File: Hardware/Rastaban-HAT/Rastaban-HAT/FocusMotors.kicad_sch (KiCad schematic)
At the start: 10 parts, among them U6 TMC2208_Carrier, U7 DRV8838 POLOLU, U8 TLV1117-33

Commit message: enh pcb component layout
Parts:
- C14, C15, C18, C19, C24: Purpose (none) -> decoupling
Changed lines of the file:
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@@
+      (effects (font (size 1.27 1.27)) hide)
+    )
+    (property "Purpose" "decoupling" (id 4) (at 193.04 111.125 0)
       (effects (font (size 1.27 1.27)) hide)
     )
@@
       (effects (font (size 1.27 1.27)) hide)
     )
+    (property "Purpose" "decoupling" (id 4) (at 201.295 109.855 0)
+      (effects (font (size 1.27 1.27)) hide)
+    )
     (pin "1")
     (pin "2")
@@
     )
     (property "Manufacturer_Part_Number" "C525005" (id 5) (at 134.62 106.68 0)
+      (effects (font (size 1.27 1.27)) hide)
+    )
+    (property "Purpose" "decoupling" (id 6) (at 134.62 106.68 0)
       (effects (font (size 1.27 1.27)) hide)
     )
@@
       (effects (font (size 1.27 1.27)) hide)
     )
+    (property "Purpose" "decoupling" (id 4) (at 126.365 99.06 0)
+      (effects (font (size 1.27 1.27)) hide)
+    )
     (pin "1")
     (pin "2")
@@
       (effects (font (size 1.27 1.27)) hide)
     )
+    (property "Purpose" "decoupling" (id 6) (at 170.18 111.125 0)
+      (effects (font (size 1.27 1.27)) hide)
+    )

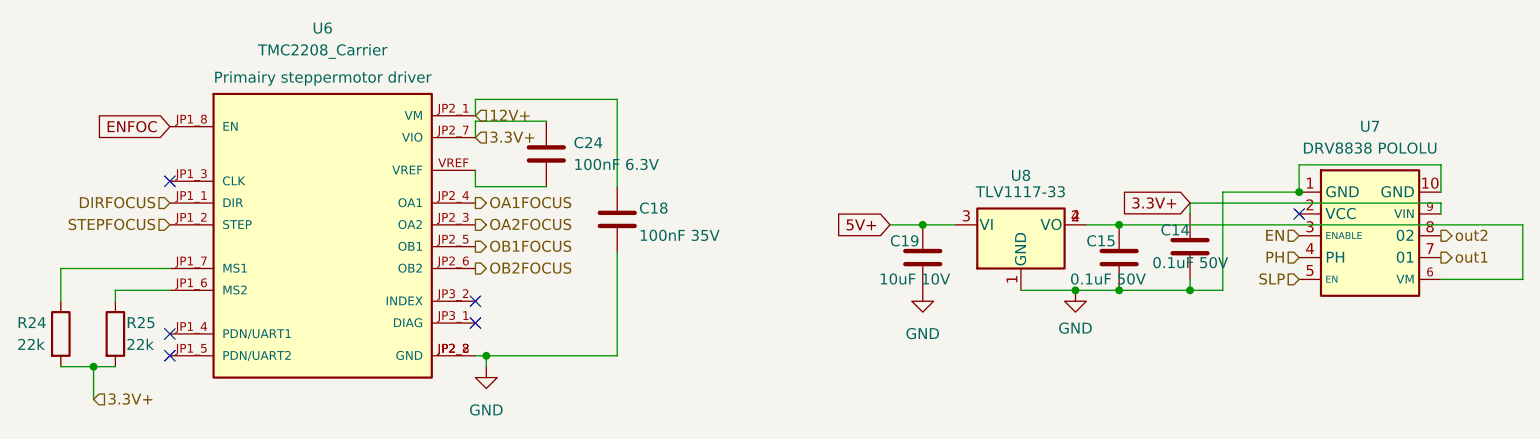
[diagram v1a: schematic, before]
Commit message: changed capacitor footprints
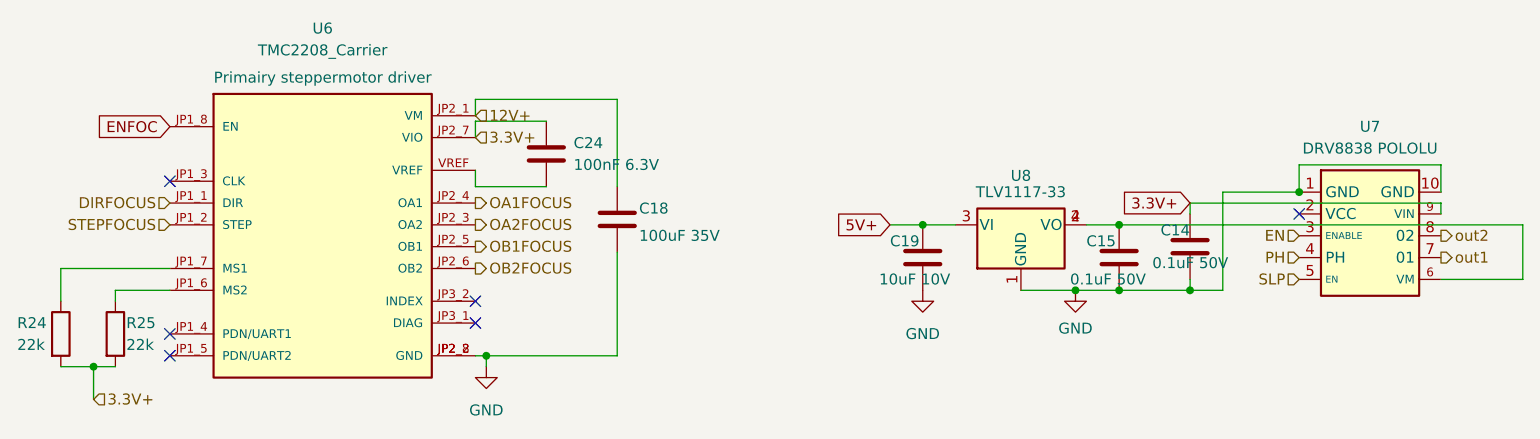
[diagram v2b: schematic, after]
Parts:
- C14, C15: footprint Capacitor_SMD:C_0805_2012Metric_Pad1.18x1.45mm_HandSolder -> Capacitor_SMD:CP_Elec_6.3x7.7
- C18: value 100nF 35V -> 100uF 35V; footprint Capacitor_THT:C_Radial_D6.3mm_H11.0mm_P2.50mm -> Capacitor_SMD:CP_Elec_8x10
- C19: footprint Capacitor_THT:C_Radial_D6.3mm_H11.0mm_P2.50mm -> Capacitor_SMD:CP_Elec_3x5.4
- C24: footprint Capacitor_SMD:C_0805_2012Metric_Pad1.18x1.45mm_HandSolder -> Capacitor_SMD:CP_Elec_4x5.4
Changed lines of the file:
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@@
       (effects (font (size 1.27 1.27)) (justify right))
     )
-    (property "Footprint" "Capacitor_SMD:C_0805_2012Metric_Pad1.18x1.45mm_HandSolder" (id 2) (at 192.0748 107.315 0)
+    (property "Footprint" "Capacitor_SMD:CP_Elec_6.3x7.7" (id 2) (at 192.0748 107.315 0)
       (effects (font (size 1.27 1.27)) hide)
     )
@@
       (effects (font (size 1.27 1.27)) (justify right))
     )
-    (property "Footprint" "Capacitor_SMD:C_0805_2012Metric_Pad1.18x1.45mm_HandSolder" (id 2) (at 202.2602 113.665 0)
+    (property "Footprint" "Capacitor_SMD:CP_Elec_6.3x7.7" (id 2) (at 202.2602 113.665 0)
       (effects (font (size 1.27 1.27)) hide)
     )
@@
       (effects (font (size 1.27 1.27)) (justify left))
     )
-    (property "Value" "100nF 35V" (id 1) (at 137.16 108.585 0)
-      (effects (font (size 1.27 1.27)) (justify left))
-    )
-    (property "Footprint" "Capacitor_THT:C_Radial_D6.3mm_H11.0mm_P2.50mm" (id 2) (at 135.5852 110.49 0)
+    (property "Value" "100uF 35V" (id 1) (at 137.16 108.585 0)
+      (effects (font (size 1.27 1.27)) (justify left))
+    )
+    (property "Footprint" "Capacitor_SMD:CP_Elec_8x10" (id 2) (at 135.5852 110.49 0)
       (effects (font (size 1.27 1.27)) hide)
     )
@@
       (effects (font (size 1.27 1.27)) (justify left))
     )
-    (property "Footprint" "Capacitor_SMD:C_0805_2012Metric_Pad1.18x1.45mm_HandSolder" (id 2) (at 127.3302 102.87 0)
+    (property "Footprint" "Capacitor_SMD:CP_Elec_4x5.4" (id 2) (at 127.3302 102.87 0)
       (effects (font (size 1.27 1.27)) hide)
     )
@@
       (effects (font (size 1.27 1.27)) (justify left))
     )
-    (property "Footprint" "Capacitor_THT:C_Radial_D6.3mm_H11.0mm_P2.50mm" (id 2) (at 171.1452 114.935 0)
-      (effects (font (size 1.27 1.27)) hide)
-    )
+    (property "Footprint" "Capacitor_SMD:CP_Elec_3x5.4" (id 2) (at 171.1452 114.935 0)
+      (effects (font (size 1.27 1.27)) hide)
+    )

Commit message: added testpoints
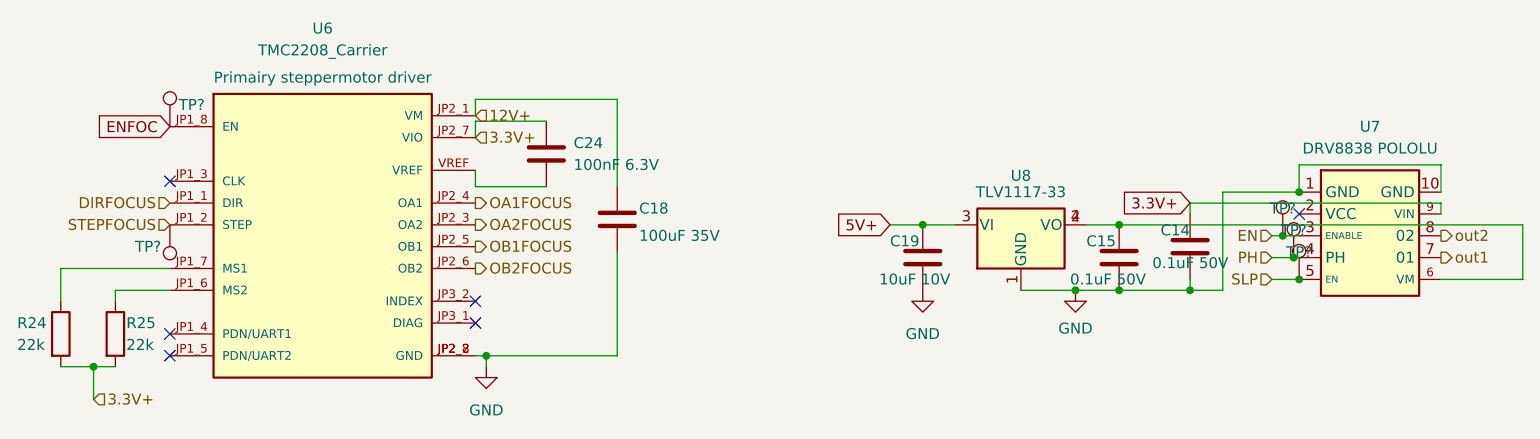
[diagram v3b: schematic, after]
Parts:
- added TP? (x5): TestPoint, TestPoint:TestPoint_THTPad_2.0x2.0mm_Drill1.0mm, symbol Connector:TestPoint
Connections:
- net EN: now also TP?.1
- net ENFOC: now also TP?.1
- net PH: now also TP?.1
- net SLP: now also TP?.1
- net STEPFOCUS: now also TP?.1
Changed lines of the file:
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@@
     (comment 1 "Casper R. Tak")
   )
+  (junction (at 213.995 113.665) (diameter 0) (color 0 0 0 0)
+  )
   (junction (at 119.38 122.555) (diameter 0) (color 0 0 0 0)
   )
@@
   (junction (at 213.995 103.505) (diameter 0) (color 0 0 0 0)
   )
+  (junction (at 212.09 108.585) (diameter 0) (color 0 0 0 0)
+  )
   (junction (at 170.18 107.315) (diameter 0) (color 0 0 0 0)
   )
   (junction (at 187.96 114.935) (diameter 0) (color 0 0 0 0)
+  )
+  (junction (at 213.36 111.125) (diameter 0) (color 0 0 0 0)
   )
   (junction (at 201.295 114.935) (diameter 0) (color 0 0 0 0)
@@
     (stroke (width 0) (type default) (color 0 0 0 0))
   )
+  (wire (pts (xy 213.36 111.125) (xy 213.995 111.125))
+    (stroke (width 0) (type default) (color 0 0 0 0))
+  )
   (wire (pts (xy 230.505 104.775) (xy 230.505 106.045))
     (stroke (width 0) (type default) (color 0 0 0 0))
@@
     (stroke (width 0) (type default) (color 0 0 0 0))
   )
+  (wire (pts (xy 212.09 108.585) (xy 213.995 108.585))
+    (stroke (width 0) (type default) (color 0 0 0 0))
+  )
   (wire (pts (xy 118.11 100.965) (xy 118.11 102.87))
     (stroke (width 0) (type default) (color 0 0 0 0))
@@
     (stroke (width 0) (type default) (color 0 0 0 0))
   )
+  (wire (pts (xy 210.82 113.665) (xy 213.995 113.665))
+    (stroke (width 0) (type default) (color 0 0 0 0))
+  )
   (wire (pts (xy 118.11 95.25) (xy 118.11 97.155))
     (stroke (width 0) (type default) (color 0 0 0 0))
@@
     (stroke (width 0) (type default) (color 0 0 0 0))
   )
+  (wire (pts (xy 210.82 111.125) (xy 213.36 111.125))
+    (stroke (width 0) (type default) (color 0 0 0 0))
+  )
   (wire (pts (xy 118.11 95.25) (xy 126.365 95.25))
     (stroke (width 0) (type default) (color 0 0 0 0))
@@
   )
   (wire (pts (xy 201.295 114.935) (xy 205.105 114.935))
+    (stroke (width 0) (type default) (color 0 0 0 0))
+  )
+  (wire (pts (xy 210.82 108.585) (xy 212.09 108.585))
     (stroke (width 0) (type default) (color 0 0 0 0))
   )
@@
     (effects (font (size 1.27 1.27)) (justify right))
   )
-  (hierarchical_label "SLP" (shape input) (at 213.995 113.665 180)
+  (hierarchical_label "SLP" (shape input) (at 210.82 113.665 180)
     (effects (font (size 1.27 1.27)) (justify right))
   )
@@
     (effects (font (size 1.27 1.27)) (justify left))
   )
-  (hierarchical_label "EN" (shape input) (at 213.995 108.585 180)
-    (effects (font (size 1.27 1.27)) (justify right))
-  )
-  (hierarchical_label "PH" (shape input) (at 213.995 111.125 180)
+  (hierarchical_label "EN" (shape input) (at 210.82 108.585 180)
+    (effects (font (size 1.27 1.27)) (justify right))
+  )
+  (hierarchical_label "PH" (shape input) (at 210.82 111.125 180)
     (effects (font (size 1.27 1.27)) (justify right))
   )
@@
     (pin "1")
     (pin "2")
+  )
+  (symbol (lib_id "Connector:TestPoint") (at 213.36 111.125 0) (unit 1)
+    (in_bom yes) (on_board yes)
+    (property "Reference" "TP?" (id 0) (at 213.36 107.95 0))
+    (property "Value" "TestPoint" (id 1) (at 213.36 106.045 0)
+      (effects (font (size 1.27 1.27)) hide)
+    )
+    (property "Footprint" "TestPoint:TestPoint_THTPad_2.0x2.0mm_Drill1.0mm" (id 2) (at 218.44 111.125 0)
+      (effects (font (size 1.27 1.27)) hide)
+    )
+    (property "Datasheet" "~" (id 3) (at 218.44 111.125 0)
+      (effects (font (size 1.27 1.27)) hide)
+    )
+    (pin "1")
   )
   (symbol (lib_id "power:GND") (at 170.18 114.935 0) (unit 1)
@@
     (pin "2")
   )
+  (symbol (lib_id "Connector:TestPoint") (at 212.09 108.585 0) (unit 1)
+    (in_bom yes) (on_board yes)
+    (property "Reference" "TP?" (id 0) (at 212.09 105.41 0))
+    (property "Value" "TestPoint" (id 1) (at 212.09 103.505 0)
+      (effects (font (size 1.27 1.27)) hide)
+    )
+    (property "Footprint" "TestPoint:TestPoint_THTPad_2.0x2.0mm_Drill1.0mm" (id 2) (at 217.17 108.585 0)
+      (effects (font (size 1.27 1.27)) hide)
+    )
+    (property "Datasheet" "~" (id 3) (at 217.17 108.585 0)
+      (effects (font (size 1.27 1.27)) hide)
+    )
+    (pin "1")
+  )
+  (symbol (lib_id "Connector:TestPoint") (at 82.55 107.315 180) (unit 1)
+    (in_bom yes) (on_board yes)
+    (property "Reference" "TP?" (id 0) (at 80.01 109.855 0))
+    (property "Value" "TestPoint" (id 1) (at 82.55 112.395 0)
+      (effects (font (size 1.27 1.27)) hide)
+    )
+    (property "Footprint" "TestPoint:TestPoint_THTPad_2.0x2.0mm_Drill1.0mm" (id 2) (at 77.47 107.315 0)
+      (effects (font (size 1.27 1.27)) hide)
+    )
+    (property "Datasheet" "~" (id 3) (at 77.47 107.315 0)
+      (effects (font (size 1.27 1.27)) hide)
+    )
+    (pin "1")
+  )
+  (symbol (lib_id "Connector:TestPoint") (at 82.55 95.885 0) (unit 1)
+    (in_bom yes) (on_board yes)
+    (property "Reference" "TP?" (id 0) (at 85.09 93.345 0))
+    (property "Value" "TestPoint" (id 1) (at 82.55 90.805 0)
+      (effects (font (size 1.27 1.27)) hide)
+    )
+    (property "Footprint" "TestPoint:TestPoint_THTPad_2.0x2.0mm_Drill1.0mm" (id 2) (at 87.63 95.885 0)
+      (effects (font (size 1.27 1.27)) hide)
+    )
+    (property "Datasheet" "~" (id 3) (at 87.63 95.885 0)
+      (effects (font (size 1.27 1.27)) hide)
+    )
+    (pin "1")
+  )
   (symbol (lib_id "Device:C") (at 126.365 99.06 0) (unit 1)
     (in_bom yes) (on_board yes) (fields_autoplaced)
@@
     (pin "2")
   )
+  (symbol (lib_id "Connector:TestPoint") (at 213.995 113.665 0) (unit 1)
+    (in_bom yes) (on_board yes)
+    (property "Reference" "TP?" (id 0) (at 213.995 110.49 0))
+    (property "Value" "TestPoint" (id 1) (at 213.995 108.585 0)
+      (effects (font (size 1.27 1.27)) hide)
+    )
+    (property "Footprint" "TestPoint:TestPoint_THTPad_2.0x2.0mm_Drill1.0mm" (id 2) (at 219.075 113.665 0)
+      (effects (font (size 1.27 1.27)) hide)
+    )
+    (property "Datasheet" "~" (id 3) (at 219.075 113.665 0)
+      (effects (font (size 1.27 1.27)) hide)
+    )
+    (pin "1")
+  )
   (symbol (lib_id "Device:R") (at 76.2 120.015 0) (unit 1)

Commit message: Removed LEDS
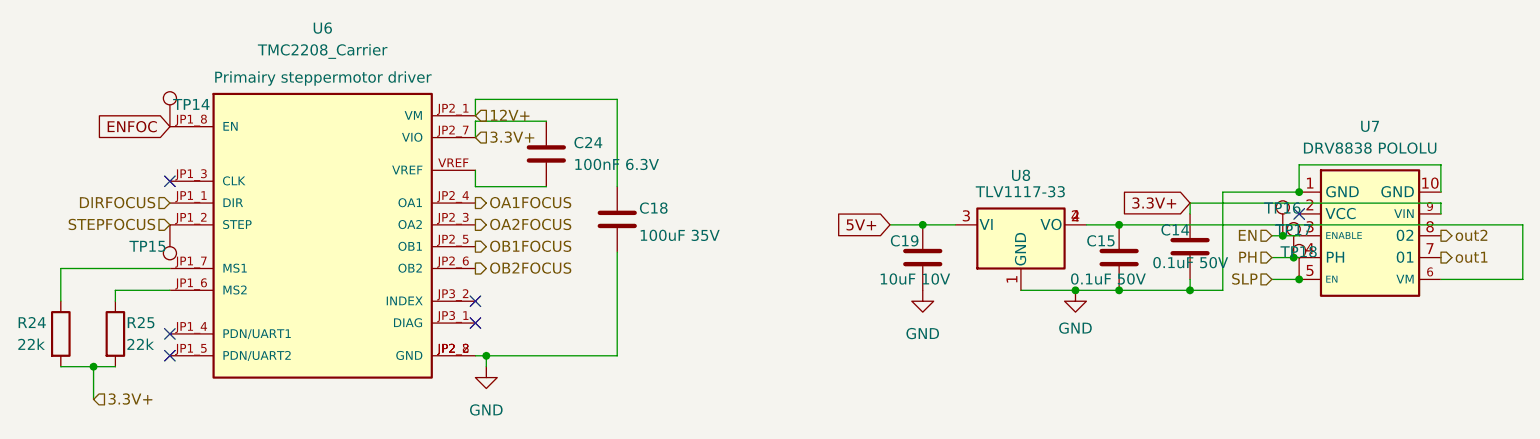
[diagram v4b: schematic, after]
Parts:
- gave numbers to parts that had none: 5
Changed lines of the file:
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@@
   (symbol (lib_id "Connector:TestPoint") (at 213.36 111.125 0) (unit 1)
     (in_bom yes) (on_board yes)
-    (property "Reference" "TP?" (id 0) (at 213.36 107.95 0))
+    (property "Reference" "TP17" (id 0) (at 213.36 107.95 0))
     (property "Value" "TestPoint" (id 1) (at 213.36 106.045 0)
       (effects (font (size 1.27 1.27)) hide)
@@
   (symbol (lib_id "Connector:TestPoint") (at 212.09 108.585 0) (unit 1)
     (in_bom yes) (on_board yes)
-    (property "Reference" "TP?" (id 0) (at 212.09 105.41 0))
+    (property "Reference" "TP16" (id 0) (at 212.09 105.41 0))
     (property "Value" "TestPoint" (id 1) (at 212.09 103.505 0)
       (effects (font (size 1.27 1.27)) hide)
@@
   (symbol (lib_id "Connector:TestPoint") (at 82.55 107.315 180) (unit 1)
     (in_bom yes) (on_board yes)
-    (property "Reference" "TP?" (id 0) (at 80.01 109.855 0))
+    (property "Reference" "TP15" (id 0) (at 80.01 109.855 0))
     (property "Value" "TestPoint" (id 1) (at 82.55 112.395 0)
       (effects (font (size 1.27 1.27)) hide)
@@
   (symbol (lib_id "Connector:TestPoint") (at 82.55 95.885 0) (unit 1)
     (in_bom yes) (on_board yes)
-    (property "Reference" "TP?" (id 0) (at 85.09 93.345 0))
+    (property "Reference" "TP14" (id 0) (at 85.09 93.345 0))
     (property "Value" "TestPoint" (id 1) (at 82.55 90.805 0)
       (effects (font (size 1.27 1.27)) hide)
@@
   (symbol (lib_id "Connector:TestPoint") (at 213.995 113.665 0) (unit 1)
     (in_bom yes) (on_board yes)
-    (property "Reference" "TP?" (id 0) (at 213.995 110.49 0))
+    (property "Reference" "TP18" (id 0) (at 213.995 110.49 0))
     (property "Value" "TestPoint" (id 1) (at 213.995 108.585 0)
       (effects (font (size 1.27 1.27)) hide)

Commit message: Started changing capacitor types and sizes
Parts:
- C14: footprint Capacitor_SMD:CP_Elec_6.3x7.7 -> Capacitor_SMD:C_0805_2012Metric_Pad1.18x1.45mm_HandSolder
- C24: footprint Capacitor_SMD:CP_Elec_4x5.4 -> Capacitor_SMD:C_0805_2012Metric_Pad1.18x1.45mm_HandSolder
- U7: Vanallesenmeer (none) -> https://www.vanallesenmeer.nl/DRV8838-Single-Brushed-DC-Mot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
- U8: LCSC (none) -> C37359; Purpose (none) -> Voltage regulator
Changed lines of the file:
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@@
+      (effects (font (size 1.27 1.27)) hide)
+    )
+    (property "Vanallesenmeer" "https://www.vanallesenmeer.nl/DRV8838-Single-Brushed-DC-Motor-Driver-Carrier-Pololu-2990" (id 5) (at 222.25 106.045 0)
       (effects (font (size 1.27 1.27)) hide)
     )
@@
     (pin "2")
   )
-  (symbol (lib_id "Regulator_Linear:TLV1117-33") (at 181.61 107.315 0) (unit 1)
-    (in_bom yes) (on_board yes)
-    (property "Reference" "U8" (id 0) (at 181.61 101.6 0))
-    (property "Value" "TLV1117-33" (id 1) (at 181.61 103.505 0))
-    (property "Footprint" "SamacSys_Parts:SOT230P700X180-4N" (id 2) (at 180.975 127 0)
-      (effects (font (size 1.27 1.27)) hide)
-    )
-    (property "Datasheet" "http://www.ti.com/lit/ds/symlink/tlv1117.pdf" (id 3) (at 182.245 129.54 0)
-      (effects (font (size 1.27 1.27)) hide)
-    )
-    (pin "1")
-    (pin "2")
-    (pin "3")
-    (pin "4")
-  )
   (symbol (lib_id "Device:C") (at 201.295 109.855 0) (unit 1)
     (in_bom yes) (on_board yes)
@@
       (effects (font (size 1.27 1.27)) (justify right))
     )
-    (property "Footprint" "Capacitor_SMD:CP_Elec_6.3x7.7" (id 2) (at 202.2602 113.665 0)
+    (property "Footprint" "Capacitor_SMD:C_0805_2012Metric_Pad1.18x1.45mm_HandSolder" (id 2) (at 202.2602 113.665 0)
       (effects (font (size 1.27 1.27)) hide)
     )
@@
     (pin "2")
   )
+  (symbol (lib_id "Regulator_Linear:TLV1117-33") (at 181.61 107.315 0) (unit 1)
+    (in_bom yes) (on_board yes)
+    (property "Reference" "U8" (id 0) (at 181.61 101.6 0))
+    (property "Value" "TLV1117-33" (id 1) (at 181.61 103.505 0))
+    (property "Footprint" "SamacSys_Parts:SOT230P700X180-4N" (id 2) (at 180.975 127 0)
+      (effects (font (size 1.27 1.27)) hide)
+    )
+    (property "Datasheet" "http://www.ti.com/lit/ds/symlink/tlv1117.pdf" (id 3) (at 182.245 129.54 0)
+      (effects (font (size 1.27 1.27)) hide)
+    )
+    (property "LCSC" "C37359" (id 5) (at 181.61 107.315 0)
+      (effects (font (size 1.27 1.27)) hide)
+    )
+    (property "Purpose" "Voltage regulator" (id 6) (at 181.61 107.315 0)
+      (effects (font (size 1.27 1.27)) hide)
+    )
+    (pin "1")
+    (pin "2")
+    (pin "3")
+    (pin "4")
+  )
   (symbol (lib_id "Connector:TestPoint") (at 212.09 108.585 0) (unit 1)
     (in_bom yes) (on_board yes)
@@
       (effects (font (size 1.27 1.27)) (justify left))
     )
-    (property "Footprint" "Capacitor_SMD:CP_Elec_4x5.4" (id 2) (at 127.3302 102.87 0)
-      (effects (font (size 1.27 1.27)) hide)
-    )
+    (property "Footprint" "Capacitor_SMD:C_0805_2012Metric_Pad1.18x1.45mm_HandSolder" (id 2) (at 127.3302 102.87 0)
+      (effects (font (size 1.27 1.27)) hide)
+    )
